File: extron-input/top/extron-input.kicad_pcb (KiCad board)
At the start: 2 copper layers, 91 x 65 mm, 22 parts, among them J1 SCART-F, J10 Conn_01x01, J11 RED, J12 BLUE, J13 SYNC, J2 RED, J3 GREEN, J4 BLUE, J5 SYNC, J6 PHOENIX, J7 SENSE, J8 Conn_01x01, J9 Conn_01x01, SW1 SW_DPDT_x2, U1 LM1881

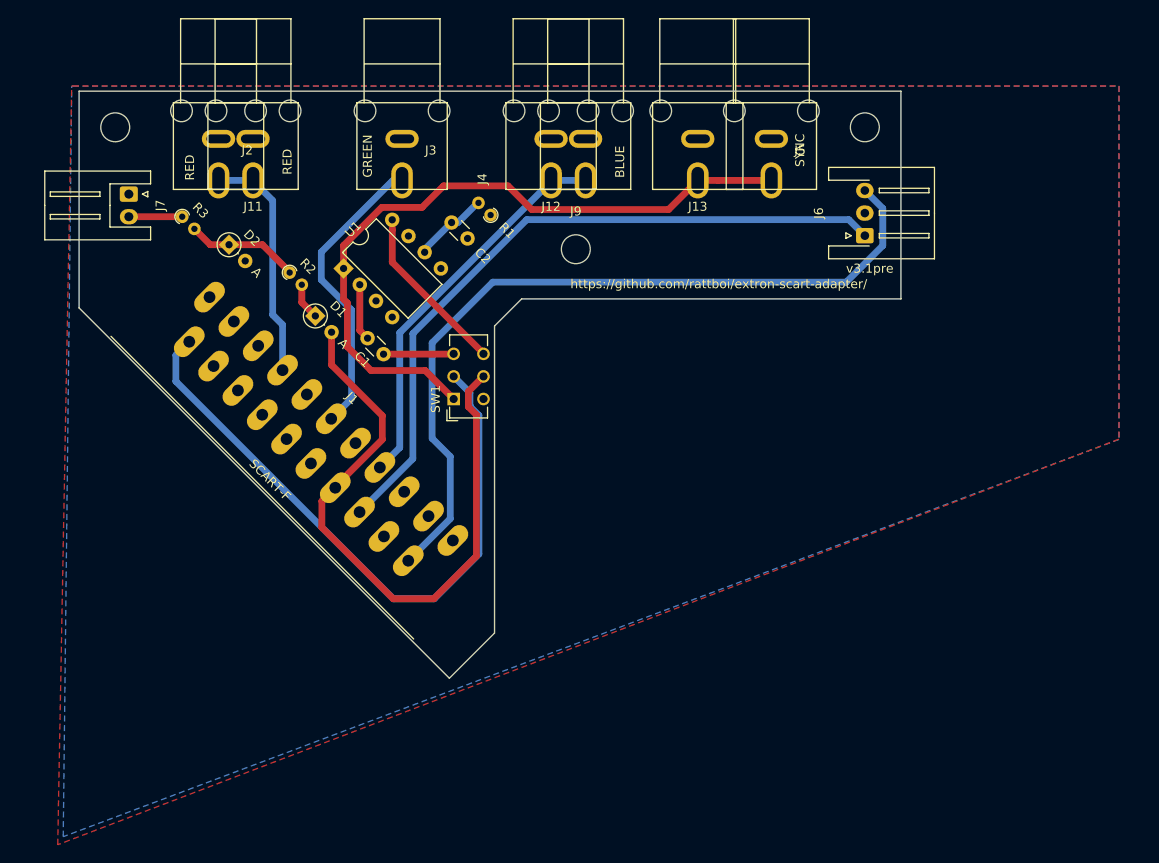
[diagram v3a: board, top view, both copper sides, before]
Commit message: Found a size for the bottom board that won't impede on the top board
These prototypes are sent off to JLC, so I'm also capturing the gerbers
in the repo.

V3.1pre

I think these have a good chance to be good...
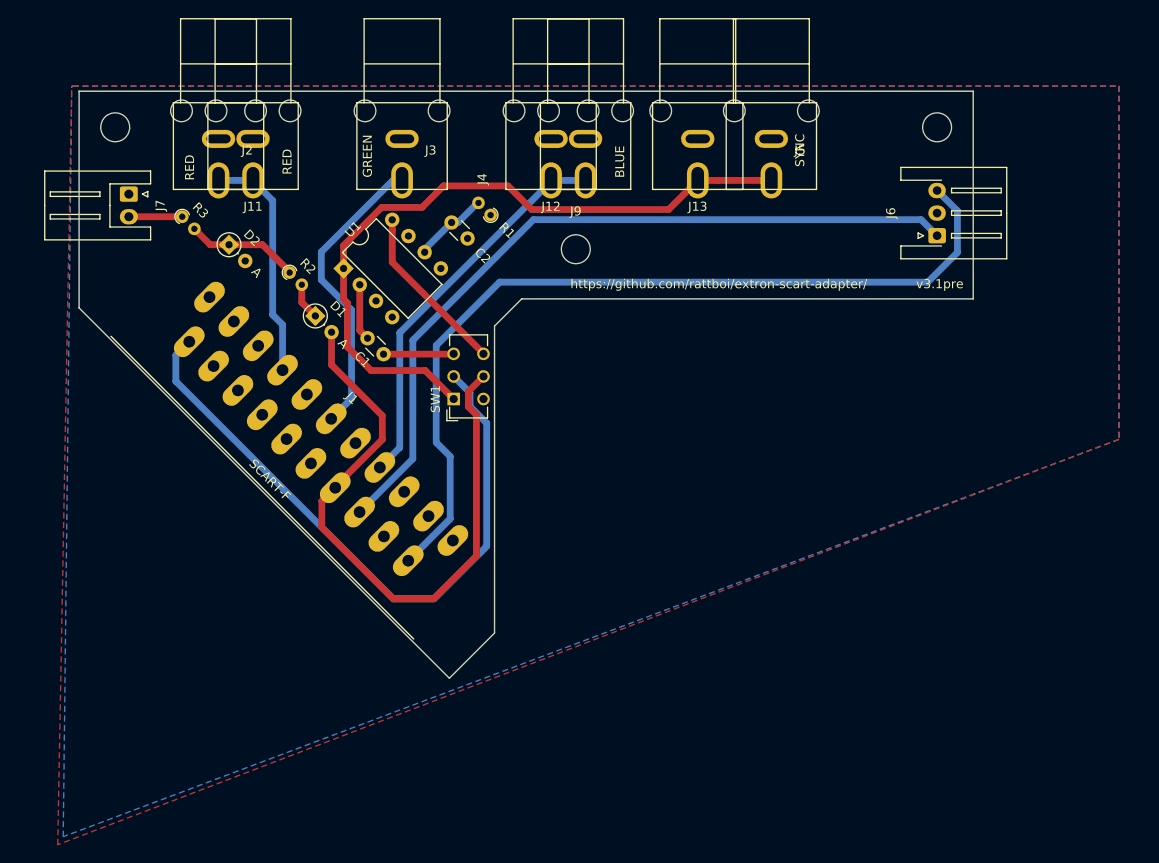
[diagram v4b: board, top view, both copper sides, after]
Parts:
- moved J6 8.00 mm to (171.0, 92.0)
- moved J8 8.00 mm to (171.0, 80.0)
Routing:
- net Net-(J1-Pad2): track 88.2 -> 96.2 mm
- net Net-(J1-Pad6): track 78.2 -> 85.8 mm
- net Net-(J1-Pad20): track 71.5 -> 72.2 mm
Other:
- board size 91 x 65 mm -> 99 x 65 mm
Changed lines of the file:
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@@
   )
   (module Connector_JST:JST_XH_S3B-XH-A-1_1x03_P2.50mm_Horizontal (layer F.Cu)
-    (at 163 92 90)
+    (at 171 92 90)
     (descr "JST XH series connector, S3B-XH-A-1 (http://www.jst-mfg.com/product/pdf/eng/eXH.pdf), generated with kicad-footprint-generator")
     (tags "connector JST XH horizontal")
@@
   )
   (module MountingHole:MountingHole_3.2mm_M3 (layer F.Cu)
-    (at 163 80)
+    (at 171 80)
     (descr "Mounting Hole 3.2mm, no annular, M3")
     (tags "mounting hole 3.2mm no annular m3")
@@
   (gr_line (start 125 99) (end 122 102) (layer Edge.Cuts) (width 0.15))
   (gr_line (start 122 136) (end 117 141) (layer Edge.Cuts) (width 0.15))
-  (gr_line (start 125 99) (end 167 99) (layer Edge.Cuts) (width 0.15))
+  (gr_line (start 125 99) (end 175 99) (layer Edge.Cuts) (width 0.15))
   (gr_line (start 122 136) (end 122 102) (layer Edge.Cuts) (width 0.15))
-  (gr_text v3.1pre (at 163.54552 95.63608) (layer F.SilkS)
+  (gr_text v3.1pre (at 171.2976 97.35312) (layer F.SilkS)
     (effects (font (size 1 1) (thickness 0.25)))
   )
@@
     (effects (font (size 1 1) (thickness 0.15)))
   )
-  (gr_line (start 76 76) (end 167 76) (layer Edge.Cuts) (width 0.15))
+  (gr_line (start 76 76) (end 175 76) (layer Edge.Cuts) (width 0.15))
   (gr_line (start 76 100) (end 76 76) (layer Edge.Cuts) (width 0.15))
   (gr_line (start 117 141) (end 76 100) (layer Edge.Cuts) (width 0.15))
-  (gr_line (start 167 76) (end 167 99) (layer Edge.Cuts) (width 0.15))
+  (gr_line (start 175 76) (end 175 99) (layer Edge.Cuts) (width 0.15))
   (segment (start 91.44 85.88) (end 91.722 85.88) (width 0.75) (layer B.Cu) (net 2))
   (segment (start 91.44 85.88) (end 95.26 85.88) (width 0.75) (layer B.Cu) (net 2))
@@
   (segment (start 128.26 85.992002) (end 128.26 85.88) (width 0.75) (layer B.Cu) (net 5))
   (segment (start 111.506 115.460015) (end 111.506 102.746002) (width 0.75) (layer B.Cu) (net 5))
-  (segment (start 119.2784 109.387) (end 117.475 107.5836) (width 0.75) (layer B.Cu) (net 12))
   (segment (start 119.2784 110.78464) (end 119.2784 109.387) (width 0.75) (layer B.Cu) (net 12))
-  (segment (start 120.269 111.89716) (end 119.21744 110.8456) (width 0.75) (layer B.Cu) (net 12))
-  (segment (start 119.21744 110.8456) (end 119.2784 110.78464) (width 0.75) (layer B.Cu) (net 12))
-  (segment (start 86.714184 108.126384) (end 110.7948 132.207) (width 0.75) (layer B.Cu) (net 12))
-  (segment (start 86.714184 105.228832) (end 86.714184 108.126384) (width 0.75) (layer B.Cu) (net 12))
+  (segment (start 121.1326 112.76076) (end 119.21744 110.8456) (width 0.75) (layer B.Cu) (net 12))
   (segment (start 88.199108 103.743908) (end 86.714184 105.228832) (width 0.75) (layer B.Cu) (net 12))
   (segment (start 110.7948 132.207) (end 115.316 132.207) (width 0.75) (layer B.Cu) (net 12))
-  (segment (start 115.316 132.207) (end 120.269 127.254) (width 0.75) (layer B.Cu) (net 12))
-  (segment (start 120.269 127.254) (end 120.269 111.89716) (width 0.75) (layer B.Cu) (net 12))
-  (segment (start 164.98824 88.98824) (end 163 87) (width 0.75) (layer B.Cu) (net 13))
-  (segment (start 164.98824 93.08972) (end 164.98824 88.98824) (width 0.75) (layer B.Cu) (net 13))
-  (segment (start 160.93312 97.14484) (end 164.98824 93.08972) (width 0.75) (layer B.Cu) (net 13))
+  (segment (start 119.2784 109.387) (end 117.475 107.5836) (width 0.75) (layer B.Cu) (net 12))
+  (segment (start 86.714184 105.228832) (end 86.714184 108.126384) (width 0.75) (layer B.Cu) (net 12))
+  (segment (start 86.714184 108.126384) (end 110.7948 132.207) (width 0.75) (layer B.Cu) (net 12))
+  (segment (start 119.21744 110.8456) (end 119.2784 110.78464) (width 0.75) (layer B.Cu) (net 12))
+  (segment (start 115.316 132.207) (end 121.1326 126.3904) (width 0.75) (layer B.Cu) (net 12))
+  (segment (start 121.1326 126.3904) (end 121.1326 112.76076) (width 0.75) (layer B.Cu) (net 12))
+  (segment (start 173.2534 93.853) (end 173.2534 89.2534) (width 0.75) (layer B.Cu) (net 13))
+  (segment (start 169.96156 97.14484) (end 173.2534 93.853) (width 0.75) (layer B.Cu) (net 13))
+  (segment (start 173.2534 89.2534) (end 171 87) (width 0.75) (layer B.Cu) (net 13))
+  (segment (start 117.094 123.3424) (end 117.094 116.44884) (width 0.75) (layer B.Cu) (net 13))
   (segment (start 112.4458 127.9906) (end 117.094 123.3424) (width 0.75) (layer B.Cu) (net 13))
-  (segment (start 117.094 116.44884) (end 115.0874 114.44224) (width 0.75) (layer B.Cu) (net 13))
-  (segment (start 115.0874 114.44224) (end 115.0874 103.86568) (width 0.75) (layer B.Cu) (net 13))
-  (segment (start 117.094 123.3424) (end 117.094 116.44884) (width 0.75) (layer B.Cu) (net 13))
-  (segment (start 121.80824 97.14484) (end 160.93312 97.14484) (width 0.75) (layer B.Cu) (net 13))
-  (segment (start 115.0874 103.86568) (end 121.80824 97.14484) (width 0.75) (layer B.Cu) (net 13))
-  (segment (start 161.22588 90.22588) (end 163 92) (width 0.75) (layer B.Cu) (net 14))
-  (segment (start 112.9538 102.83952) (end 125.56744 90.22588) (width 0.75) (layer B.Cu) (net 14))
+  (segment (start 117.094 116.44884) (end 115.5446 114.89944) (width 0.75) (layer B.Cu) (net 13))
+  (segment (start 115.5446 104.1654) (end 122.56516 97.14484) (width 0.75) (layer B.Cu) (net 13))
+  (segment (start 115.5446 114.89944) (end 115.5446 104.1654) (width 0.75) (layer B.Cu) (net 13))
+  (segment (start 122.56516 97.14484) (end 169.96156 97.14484) (width 0.75) (layer B.Cu) (net 13))
+  (segment (start 169.22588 90.22588) (end 171 92) (width 0.75) (layer B.Cu) (net 14))
+  (segment (start 126.30912 90.22588) (end 169.22588 90.22588) (width 0.75) (layer B.Cu) (net 14))
+  (segment (start 112.9538 103.5812) (end 126.30912 90.22588) (width 0.75) (layer B.Cu) (net 14))
   (segment (start 107.057646 122.602446) (end 112.9538 116.706292) (width 0.75) (layer B.Cu) (net 14))
-  (segment (start 125.56744 90.22588) (end 161.22588 90.22588) (width 0.75) (layer B.Cu) (net 14))
-  (segment (start 112.9538 116.706292) (end 112.9538 102.83952) (width 0.75) (layer B.Cu) (net 14))
+  (segment (start 112.9538 116.706292) (end 112.9538 103.5812) (width 0.75) (layer B.Cu) (net 14))
   (segment (start 114.263256 93.518904) (end 117.24132 90.54084) (width 0.75) (layer B.Cu) (net 15))
   (segment (start 114.263256 93.834949) (end 114.263256 93.518904) (width 0.75) (layer B.Cu) (net 15))

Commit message: extron-input v3
Extended bottom board by 5mm
Fixed silkscreen up to be reasonable
Fixed up gitignore
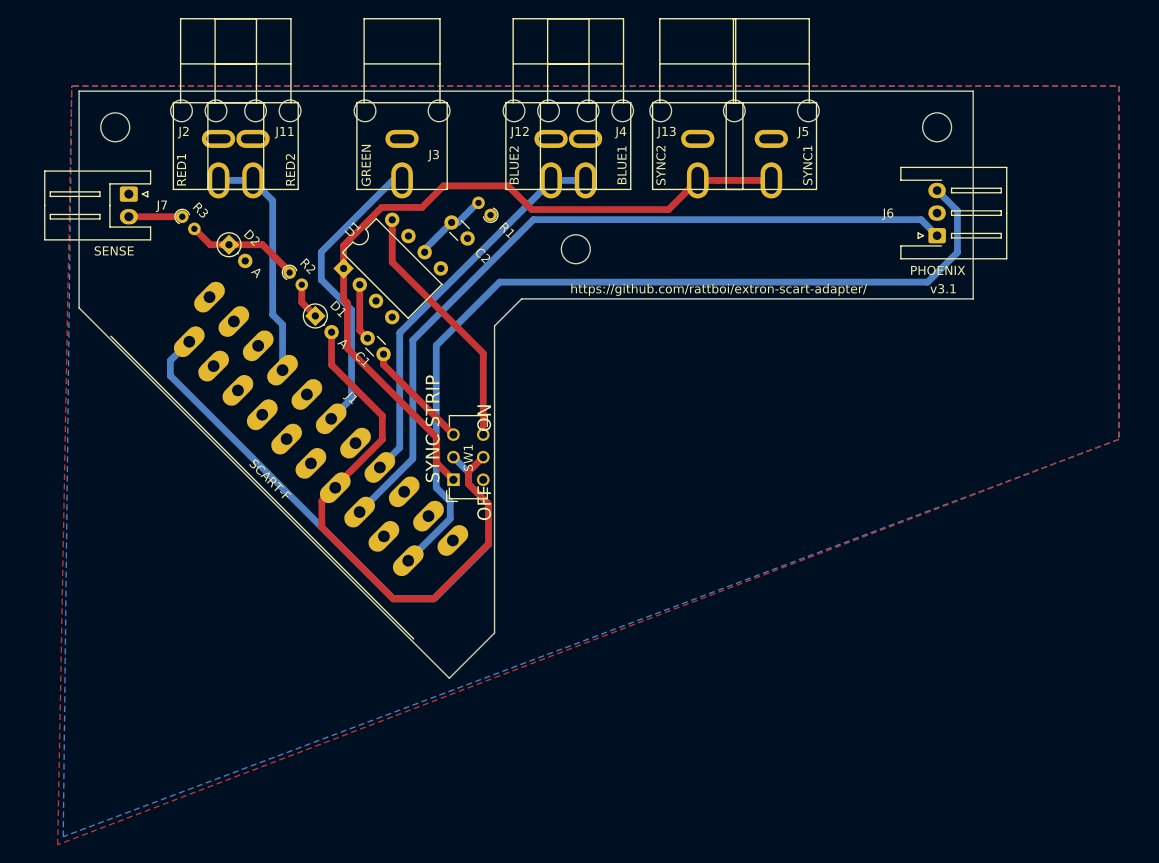
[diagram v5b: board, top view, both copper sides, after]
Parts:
- J11: value RED -> RED2
- J12: value BLUE -> BLUE2
- J13: value SYNC -> SYNC2
- J2: value RED -> RED1
- J4: value BLUE -> BLUE1
- J5: value SYNC -> SYNC1
- moved SW1 8.94 mm to (117.4, 119.0)
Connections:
- J1 pad 1: Net-(J1-Pad1) -> (no net)
- J1 pad 10: Net-(J1-Pad10) -> (no net)
- J1 pad 12: Net-(J1-Pad12) -> (no net)
- J1 pad 16: Net-(J1-Pad16) -> (no net)
- J1 pad 19: Net-(J1-Pad19) -> (no net)
- J1 pad 3: Net-(J1-Pad3) -> (no net)
- J10 pad 1: Net-(J10-Pad1) -> (no net)
- J8 pad 1: Net-(J8-Pad1) -> (no net)
- J9 pad 1: Net-(J9-Pad1) -> (no net)
- SW1 pad 4: Net-(SW1-Pad4) -> (no net)
- U1 pad 3: Net-(U1-Pad3) -> (no net)
- U1 pad 5: Net-(U1-Pad5) -> (no net)
- U1 pad 7: Net-(U1-Pad7) -> (no net)
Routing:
- net Net-(SW1-Pad6): track 19.1 -> 28.0 mm
- net Net-(J1-Pad20): track 72.2 -> 63.9 mm
- net SENSE: track 70.0 -> 62.2 mm
- net SYNC: track 80.0 -> 85.4 mm
- net Net-(C1-Pad1): track 8.19 -> 12.3 mm
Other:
- board text added: "OFF ON"
- board text added: "PHOENIX"
- board text added: "SYNC STRIP"
- board text added: "v3.1"
- board text removed: "v3.1pre"
